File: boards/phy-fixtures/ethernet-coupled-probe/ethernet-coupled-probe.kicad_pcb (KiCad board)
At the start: 4 copper layers, 108.2 x 63 mm, 61 parts, among them J1 RJ45, J10 SMA, J11 SMA, J12 SMA, J13 SMA, J14 SMA, J15 SMA, J16 SMA, J17 SMA, J18 SMA, J2 RJ45, J3 SMA, J4 SMA, J5 SMA, J6 SMA, J7 SMA, J8 SMA, J9 SMA, U1 DBTC16-282LX+, U10 DBTC16-282LX+, U11 DBTC16-282LX+, U12 DBTC16-282LX+, U13 DBTC16-282LX+, U14 DBTC16-282LX+, U15 DBTC16-282LX+, U16 DBTC16-282LX+, U2 DBTC16-282LX+, U3 DBTC16-282LX+, U4 DBTC16-282LX+, U5 DBTC16-282LX+, U6 DBTC16-282LX+, U7 DBTC16-282LX+, U8 DBTC16-282LX+, U9 DBTC16-282LX+

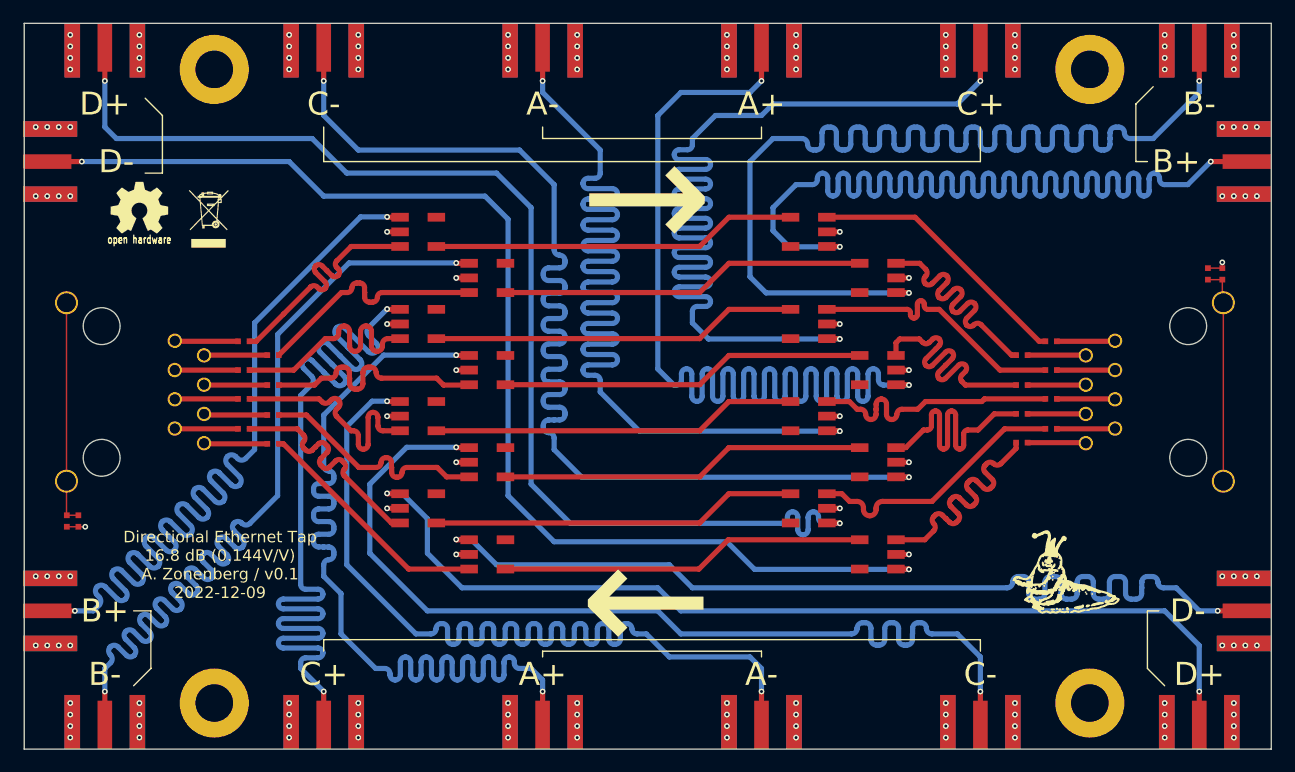
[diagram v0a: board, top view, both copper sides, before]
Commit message: Added second ground plane and stitching vias
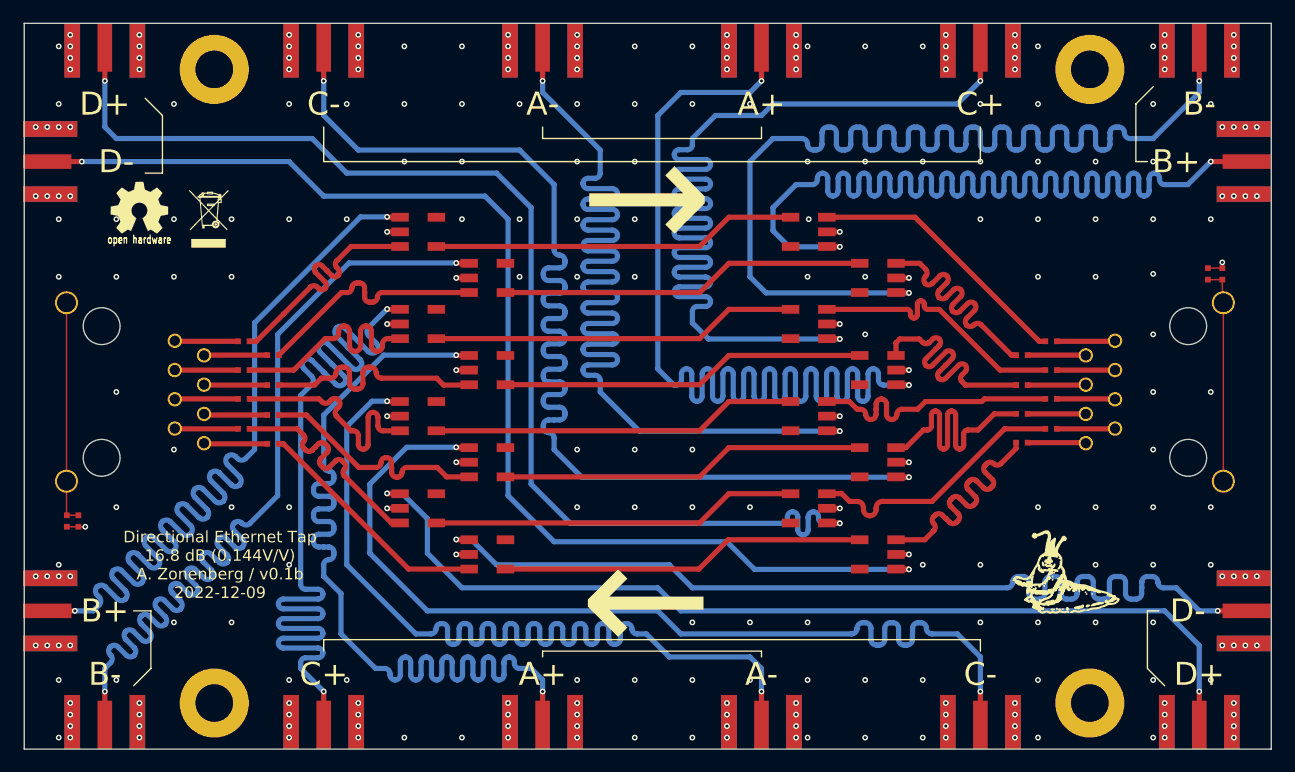
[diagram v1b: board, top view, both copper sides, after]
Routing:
- net /GND: vias 146 -> 271
- added copper zone on In2.Cu, net /GND
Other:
- board text added: "Directional Ethernet Tap 16.8 dB (0.144V/V) A. Zonenberg / v0.1b 2022-12-09"
- board text removed: "Directional Ethernet Tap 16.8 dB (0.144V/V) A. Zonenberg / v0.1 2022-12-09"

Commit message: Updated ethernet-coupled-probe for v0.2 with correct coupler footprint
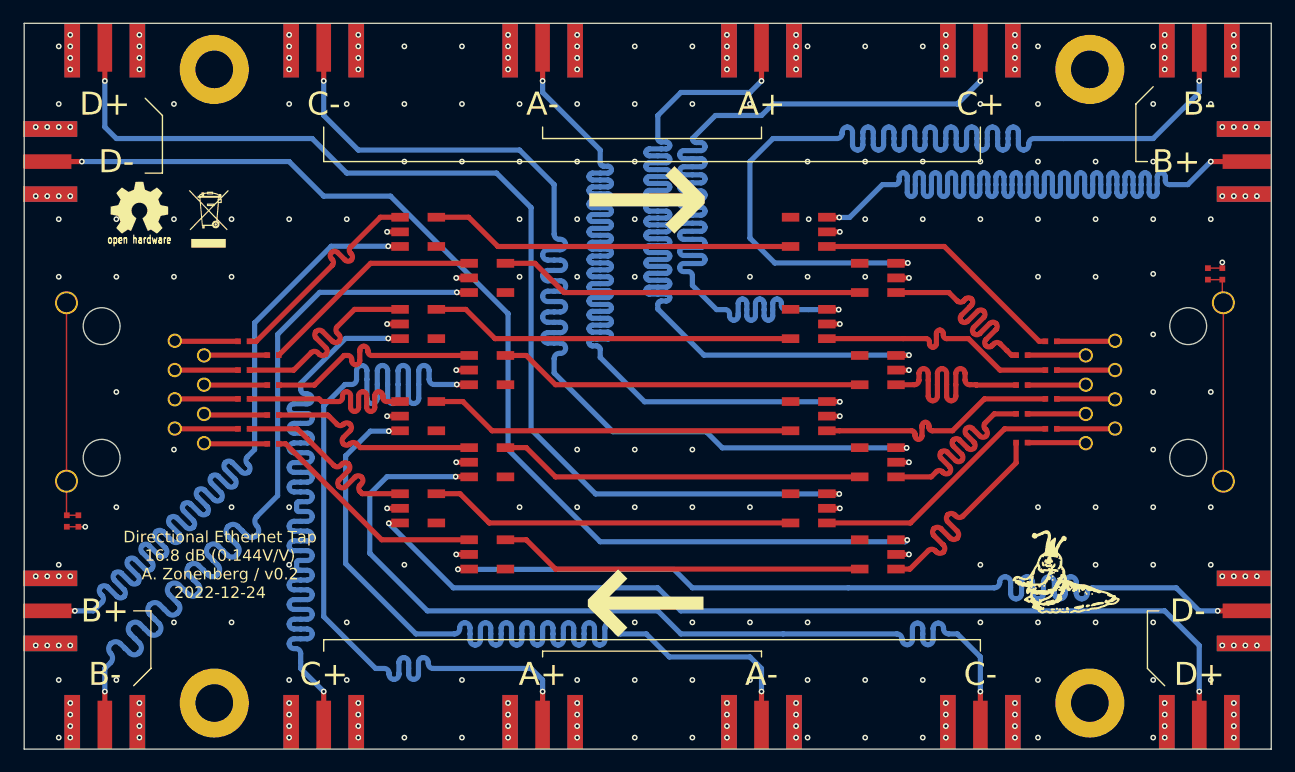
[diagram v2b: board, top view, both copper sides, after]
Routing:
- net /PAIRC_L2R_P: track 104.1 -> 95.5 mm
- net /PAIRD_L2R_N: track 104.7 -> 96.3 mm
- net /PAIRC_L2R_N: track 104.1 -> 95.8 mm
- net /PAIRA_L2R_N: track 103.9 -> 95.6 mm
- net /PAIRA_L2R_P: track 103.9 -> 95.6 mm
- net /PAIRB_L2R_N: track 103.8 -> 95.5 mm
- net /PAIRD_L2R_P: track 104.5 -> 96.2 mm
- net /PAIRB_L2R_P: track 103.4 -> 95.3 mm
- net /PAIRC_R2L_P: track 85.2 -> 79.8 mm
- net /PAIRB_R2L_P: track 85.0 -> 81.8 mm
- net /PAIRD_R2L_P: track 85.8 -> 82.6 mm
- net /PAIRD_R2L_N: track 85.4 -> 82.3 mm
- net /PAIRC_R2L_N: track 85.6 -> 82.4 mm
- net /PAIRA_R2L_N: track 85.1 -> 82.0 mm
- net /PAIRB_R2L_N: track 85.0 -> 82.0 mm
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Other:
- board text added: "Directional Ethernet Tap 16.8 dB (0.144V/V) A. Zonenberg / v0.2 2022-12-24"
- board text removed: "Directional Ethernet Tap 16.8 dB (0.144V/V) A. Zonenberg / v0.1b 2022-12-09"

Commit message: ethernet-coupled-probe: updated silkscreen and schematic with new net names for correct pinout. No changes to copper geometry.
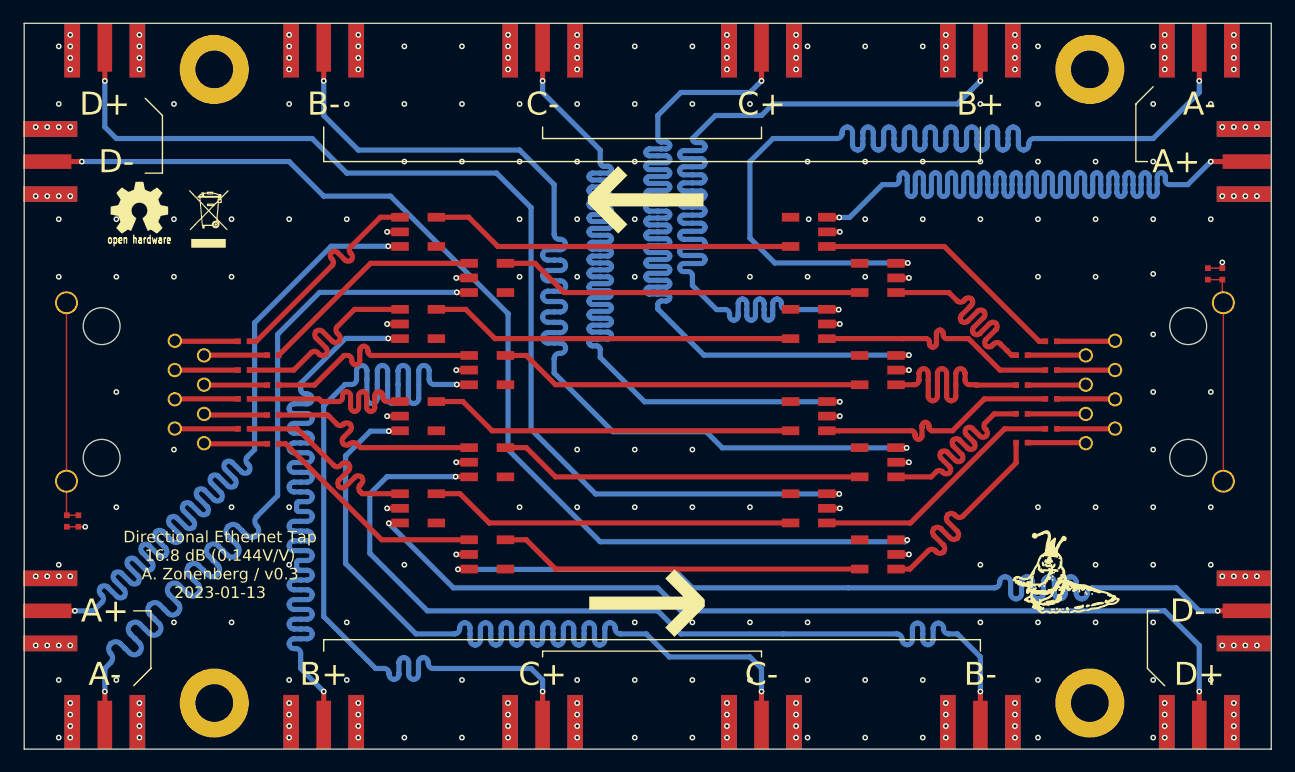
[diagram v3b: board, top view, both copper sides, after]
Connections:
- C1 pad 1: /PAIRA_L_P -> /PAIRC_R_P
- C10 pad 1: /PAIRA_R_N -> /PAIRC_L_N
- C11 pad 1: /PAIRB_R_P -> /PAIRA_L_P
- C12 pad 1: /PAIRB_R_N -> /PAIRA_L_N
- C13 pad 1: /PAIRC_R_P -> /PAIRB_L_P
- C14 pad 1: /PAIRC_R_N -> /PAIRB_L_N
- C15 pad 1: /PAIRD_R_P -> /PAIRD_L_P
- C16 pad 1: /PAIRD_R_N -> /PAIRD_L_N
- C2 pad 1: /PAIRA_L_N -> /PAIRC_R_N
- C3 pad 1: /PAIRB_L_P -> /PAIRA_R_P
- C4 pad 1: /PAIRB_L_N -> /PAIRA_R_N
- C5 pad 1: /PAIRC_L_P -> /PAIRB_R_P
- C6 pad 1: /PAIRC_L_N -> /PAIRB_R_N
- C7 pad 1: /PAIRD_L_P -> /PAIRD_R_P
- C8 pad 1: /PAIRD_L_N -> /PAIRD_R_N
- C9 pad 1: /PAIRA_R_P -> /PAIRC_L_P
- J1 pad 1: /PAIRB_L_P -> /PAIRA_R_P
- J1 pad 2: /PAIRB_L_N -> /PAIRA_R_N
- J1 pad 3: /PAIRC_L_P -> /PAIRB_R_P
- J1 pad 4: /PAIRA_L_P -> /PAIRC_R_P
- J1 pad 5: /PAIRA_L_N -> /PAIRC_R_N
- J1 pad 6: /PAIRC_L_N -> /PAIRB_R_N
- J1 pad 7: /PAIRD_L_P -> /PAIRD_R_P
- J1 pad 8: /PAIRD_L_N -> /PAIRD_R_N
- J10 pad 1: /PAIRD_L2R_N -> /PAIRD_R2L_N
- J11 pad 1: /PAIRA_R2L_P -> /PAIRC_L2R_P
- J12 pad 1: /PAIRA_R2L_N -> /PAIRC_L2R_N
- J13 pad 1: /PAIRB_R2L_P -> /PAIRA_L2R_P
- J14 pad 1: /PAIRB_R2L_N -> /PAIRA_L2R_N
- J15 pad 1: /PAIRC_R2L_P -> /PAIRB_L2R_P
- J16 pad 1: /PAIRC_R2L_N -> /PAIRB_L2R_N
- J17 pad 1: /PAIRD_R2L_P -> /PAIRD_L2R_P
- J18 pad 1: /PAIRD_R2L_N -> /PAIRD_L2R_N
- J2 pad 1: /PAIRB_R_P -> /PAIRA_L_P
- J2 pad 2: /PAIRB_R_N -> /PAIRA_L_N
- J2 pad 3: /PAIRC_R_P -> /PAIRB_L_P
- J2 pad 4: /PAIRA_R_P -> /PAIRC_L_P
- J2 pad 5: /PAIRA_R_N -> /PAIRC_L_N
- J2 pad 6: /PAIRC_R_N -> /PAIRB_L_N
- J2 pad 7: /PAIRD_R_P -> /PAIRD_L_P
- J2 pad 8: /PAIRD_R_N -> /PAIRD_L_N
- J3 pad 1: /PAIRA_L2R_P -> /PAIRC_R2L_P
- J4 pad 1: /PAIRA_L2R_N -> /PAIRC_R2L_N
- J5 pad 1: /PAIRB_L2R_P -> /PAIRA_R2L_P
- J6 pad 1: /PAIRB_L2R_N -> /PAIRA_R2L_N
- J7 pad 1: /PAIRC_L2R_P -> /PAIRB_R2L_P
- J8 pad 1: /PAIRC_L2R_N -> /PAIRB_R2L_N
- J9 pad 1: /PAIRD_L2R_P -> /PAIRD_R2L_P
- U1 pad 1: /PAIRC_L2R_P -> /PAIRB_R2L_P
- U1 pad 4: /PAIRC_MID_P -> /PAIRB_MID_P
- U10 pad 1: /PAIRC_R2L_N -> /PAIRB_L2R_N
- U10 pad 4: /PAIRC_MID_N -> /PAIRB_MID_N
- U11 pad 1: /PAIRD_R2L_P -> /PAIRD_L2R_P
- U12 pad 1: /PAIRD_R2L_N -> /PAIRD_L2R_N
- U13 pad 1: /PAIRA_R2L_P -> /PAIRC_L2R_P
- U13 pad 4: /PAIRA_MID_P -> /PAIRC_MID_P
- U14 pad 1: /PAIRA_R2L_N -> /PAIRC_L2R_N
- U14 pad 4: /PAIRA_MID_N -> /PAIRC_MID_N
- U15 pad 1: /PAIRB_R2L_P -> /PAIRA_L2R_P
- U15 pad 4: /PAIRB_MID_P -> /PAIRA_MID_P
- U16 pad 1: /PAIRB_R2L_N -> /PAIRA_L2R_N
- U16 pad 4: /PAIRB_MID_N -> /PAIRA_MID_N
- U2 pad 1: /PAIRC_L2R_N -> /PAIRB_R2L_N
- U2 pad 4: /PAIRC_MID_N -> /PAIRB_MID_N
- U3 pad 1: /PAIRD_L2R_P -> /PAIRD_R2L_P
- U4 pad 1: /PAIRD_L2R_N -> /PAIRD_R2L_N
- U5 pad 1: /PAIRA_L2R_P -> /PAIRC_R2L_P
- U5 pad 4: /PAIRA_MID_P -> /PAIRC_MID_P
- U6 pad 1: /PAIRA_L2R_N -> /PAIRC_R2L_N
- U6 pad 4: /PAIRA_MID_N -> /PAIRC_MID_N
- U7 pad 1: /PAIRB_L2R_P -> /PAIRA_R2L_P
- U7 pad 4: /PAIRB_MID_P -> /PAIRA_MID_P
- U8 pad 1: /PAIRB_L2R_N -> /PAIRA_R2L_N
- U8 pad 4: /PAIRB_MID_N -> /PAIRA_MID_N
- U9 pad 1: /PAIRC_R2L_P -> /PAIRB_L2R_P
- U9 pad 4: /PAIRC_MID_P -> /PAIRB_MID_P
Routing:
- net /PAIRC_R2L_P: track 79.8 -> 95.6 mm
- net /PAIRB_L2R_P: track 95.3 -> 79.8 mm
- net /PAIRD_R2L_N: track 82.3 -> 96.3 mm
- net /PAIRD_L2R_N: track 96.3 -> 82.3 mm
- net /PAIRA_L2R_P: track 95.6 -> 81.8 mm
- net /PAIRB_R2L_N: track 82.0 -> 95.8 mm
- net /PAIRC_L2R_N: track 95.8 -> 82.0 mm
- net /PAIRB_R2L_P: track 81.8 -> 95.5 mm
- net /PAIRD_R2L_P: track 82.6 -> 96.2 mm
- net /PAIRD_L2R_P: track 96.2 -> 82.6 mm
- net /PAIRA_L2R_N: track 95.6 -> 82.0 mm
- net /PAIRA_R2L_N: track 82.0 -> 95.5 mm
- net /PAIRC_L2R_P: track 95.5 -> 82.2 mm
- net /PAIRC_R2L_N: track 82.4 -> 95.6 mm
- net /PAIRA_R2L_P: track 82.2 -> 95.3 mm
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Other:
- board text added: "Directional Ethernet Tap 16.8 dB (0.144V/V) A. Zonenberg / v0.3 2023-01-13"
- board text removed: "Directional Ethernet Tap 16.8 dB (0.144V/V) A. Zonenberg / v0.2 2022-12-24"
